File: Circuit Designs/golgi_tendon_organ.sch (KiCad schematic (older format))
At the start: 0 parts

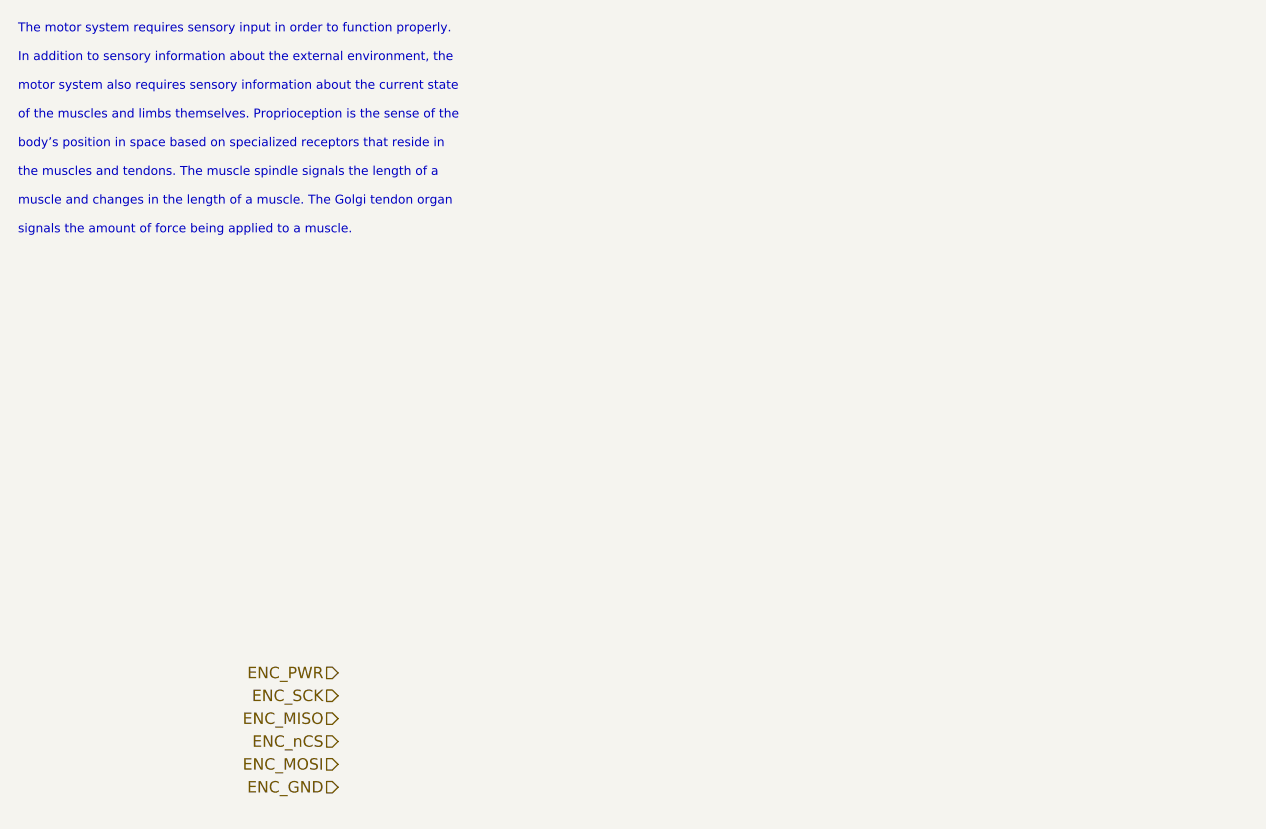
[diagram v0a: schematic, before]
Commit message: added hal sensor
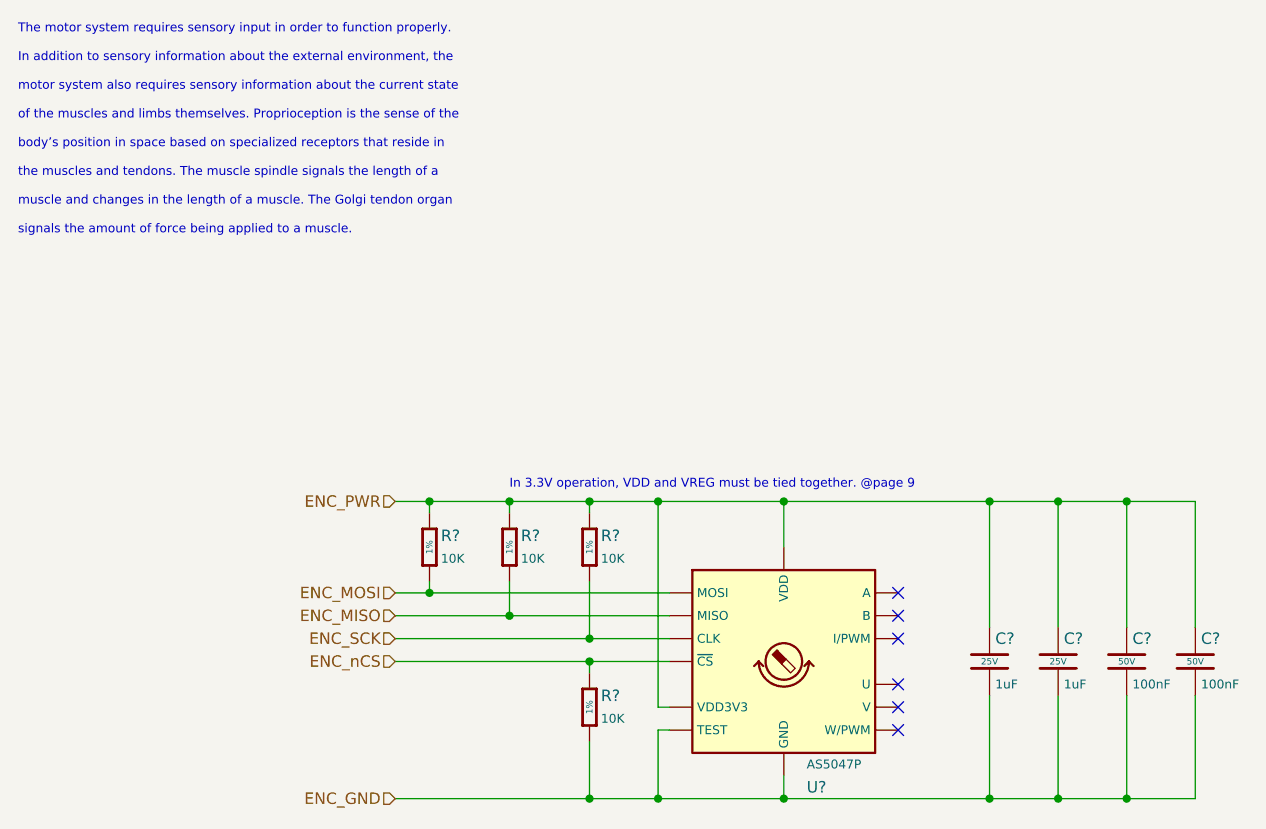
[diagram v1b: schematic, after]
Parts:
- added C? (x2): 1uF, Capacitor_SMD:C_0402_1005Metric, symbol CoE_Capacitor:1uF
- added C? (x2): 100nF, Capacitor_SMD:C_0402_1005Metric, symbol CoE_Capacitor:100nF
- added R? (x4): 10K, Resistor_SMD:R_0402_1005Metric, symbol CoE_Resistor:10K
- added U?: AS5047P, Package_SO:TSSOP-14_4.4x5mm_P0.65mm, symbol CoE_IntegratedCircuit:AS5047P
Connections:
- net ENC_GND: now also C?.2, C?.2, C?.2, C?.2, R?.2, U?.13 (GND), U?.5 (TEST)
- net ENC_MISO: now also R?.2, U?.3 (MISO)
- net ENC_MOSI: now also R?.2, U?.4 (MOSI)
- net ENC_PWR: now also C?.1, C?.1, C?.1, C?.1, R?.1, R?.1, R?.1, U?.11 (VDD), U?.12 (VDD3V3)
- net ENC_SCK: now also R?.2, U?.2 (CLK)
- net ENC_nCS: now also R?.1, U?.1 (~CS)
- no-connect marks 0 -> 6
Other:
- note added: "In 3.3V operation, VDD and VREG must be tied together. @page 9"
